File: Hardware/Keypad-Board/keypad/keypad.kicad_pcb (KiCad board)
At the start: 2 copper layers, 143 x 51 mm, 19 parts, among them J1 Conn_01x07, SW1 SW_Push_45deg, SW10 SW_Push_45deg, SW11 SW_Push_45deg, SW12 SW_Push_45deg, SW2 SW_Push_45deg, SW3 SW_Push_45deg, SW4 SW_Push_45deg, SW5 SW_Push_45deg, SW6 SW_Push_45deg, SW7 SW_Push_45deg, SW8 SW_Push_45deg, SW9 SW_Push_45deg

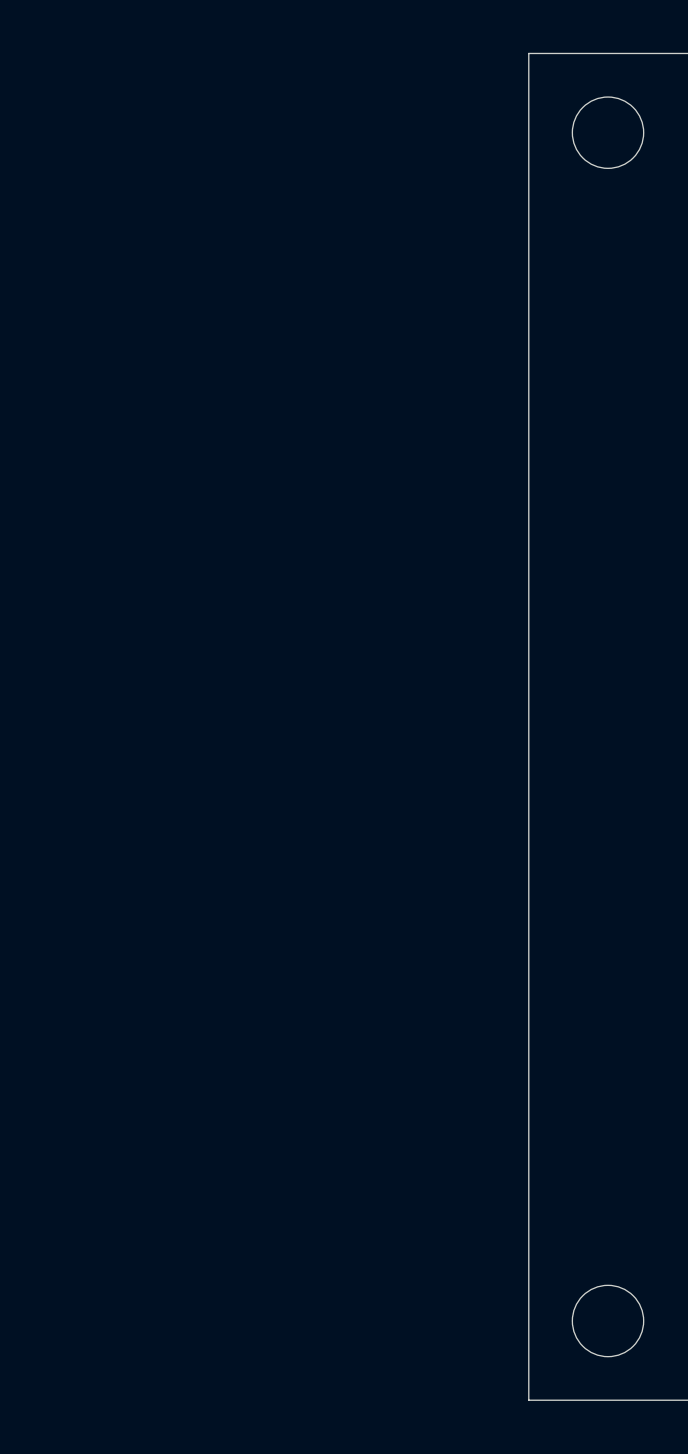
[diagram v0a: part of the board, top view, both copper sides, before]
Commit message: Add daughter board for power and reset, send to production
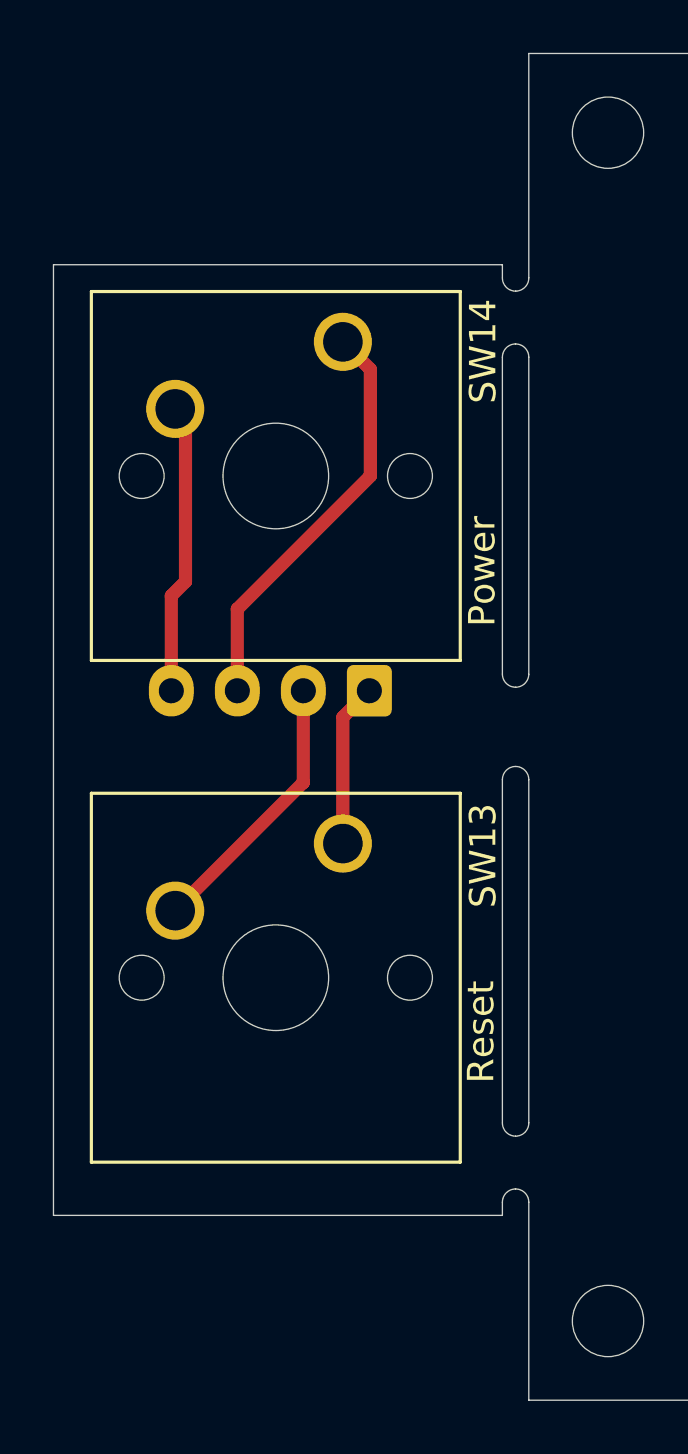
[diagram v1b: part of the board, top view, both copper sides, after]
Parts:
- added J2: Conn_01x04, Connector_JST:JST_XH_B4B-XH-A_1x04_P2.50mm_Vertical, B.Cu at (108.0, 93.1)
- added REF**: MTP Logo 5mm Low Detail, Watermarks:MTP Logo 5mm Low Detail, B.Cu at (99.0, 110.0)
- added SW13: SW_Push_45deg, Button_Switch_Keyboard:SW_Cherry_MX_1.00u_PCB, F.Cu at (107.0, 98.9)
- added SW14: SW_Push_45deg, Button_Switch_Keyboard:SW_Cherry_MX_1.00u_PCB, F.Cu at (107.0, 79.9)
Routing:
- net Net-(J2-Pin_3): track 0.00 -> 15.7 mm
- net Net-(J2-Pin_4): track 0.00 -> 11.1 mm
- net Net-(J2-Pin_2): track 0.00 -> 10.3 mm
- net Net-(J2-Pin_1): track 0.00 -> 6.20 mm
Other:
- board size 143 x 51 mm -> 161 x 51 mm
- board text added: "Michael Pate v2.0 01/2026"
- board text added: "Power"
- board text added: "Reset"
